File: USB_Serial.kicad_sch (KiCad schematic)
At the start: 1 part, among them U501 MCP2221A-I_SL

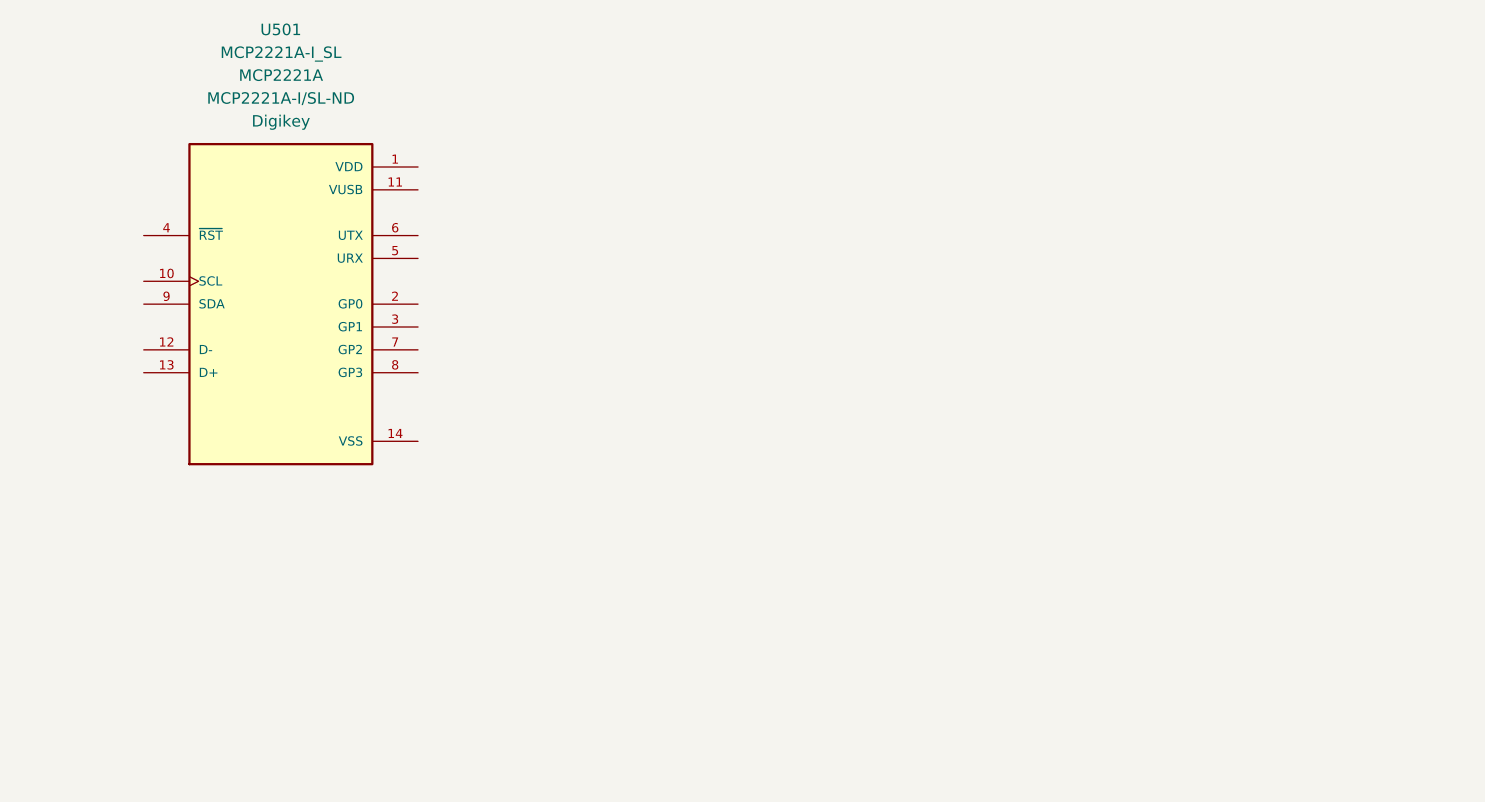
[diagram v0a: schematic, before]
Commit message: update schematic
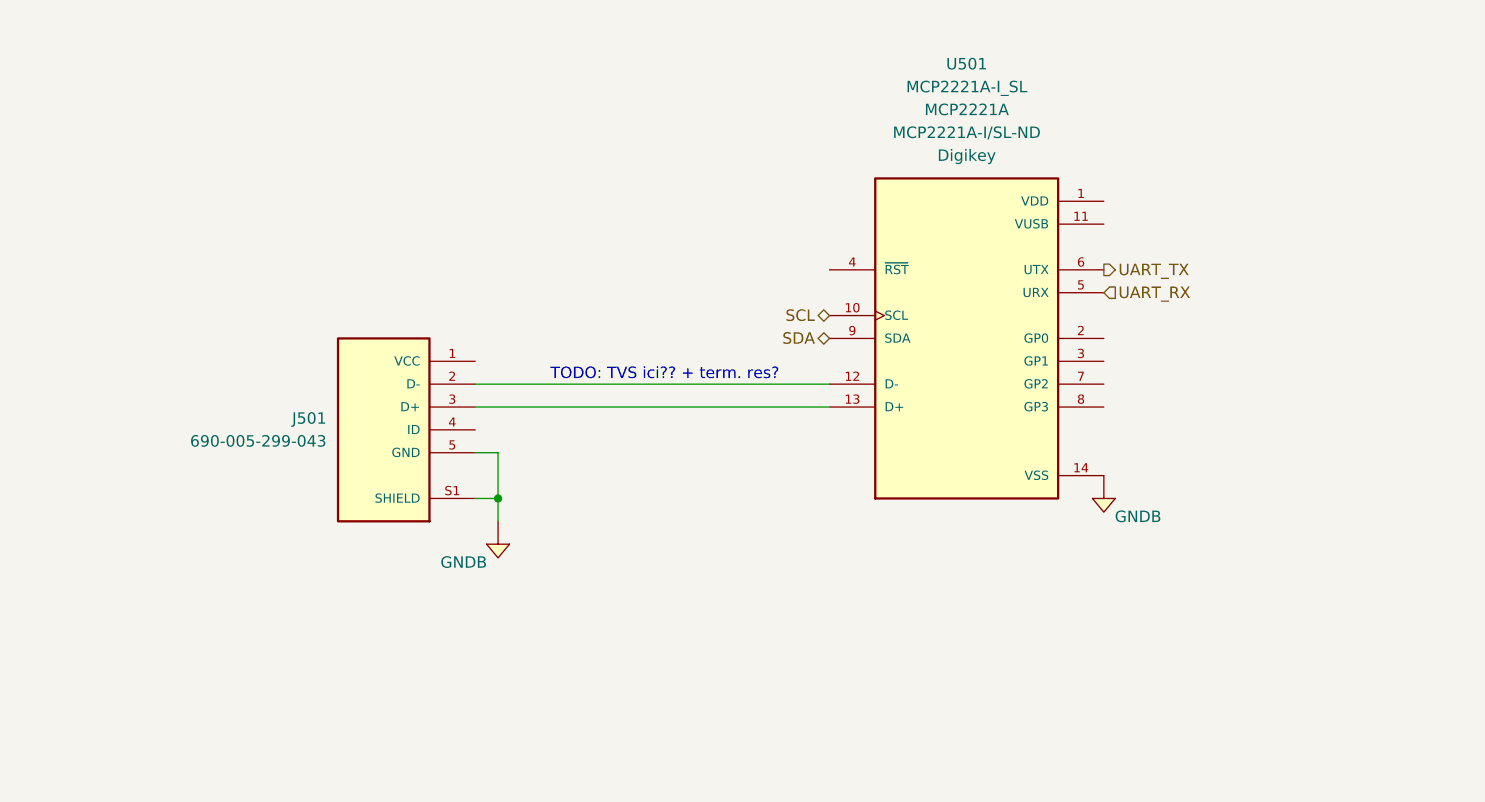
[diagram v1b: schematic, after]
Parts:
- added J501: 690-005-299-043, EDAC_690-005-299-043, symbol Connectors:690-005-299-043
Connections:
- net SCL: now reaches U501.10 (SCL)
- net at U501.12 (D-): now also J501.2 (D-)
- net at U501.13 (D+): now also J501.3 (D+)
- net GNDB: now reaches U501.14 (VSS)
- net GNDB: now also J501.5 (GND), J501.S1 (SHIELD)
- net UART_RX: now reaches U501.5 (URX)
- net UART_TX: now reaches U501.6 (UTX)
- net SDA: now reaches U501.9 (SDA)
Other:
- note added: "TODO: TVS ici?? + term. res?"
- moved on the sheet: U501

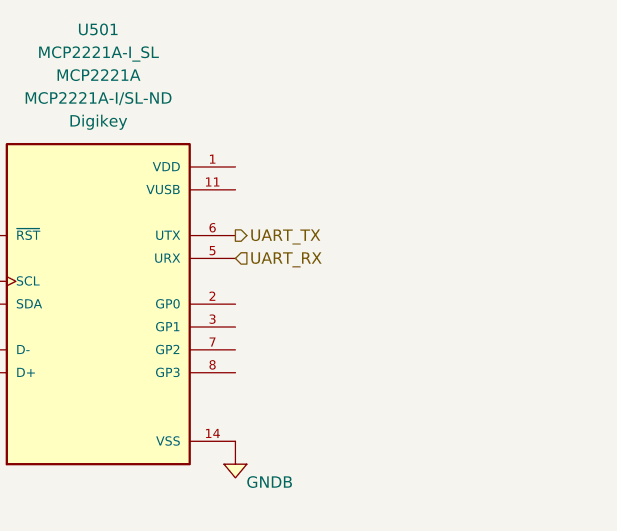
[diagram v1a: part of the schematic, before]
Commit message: update schematic
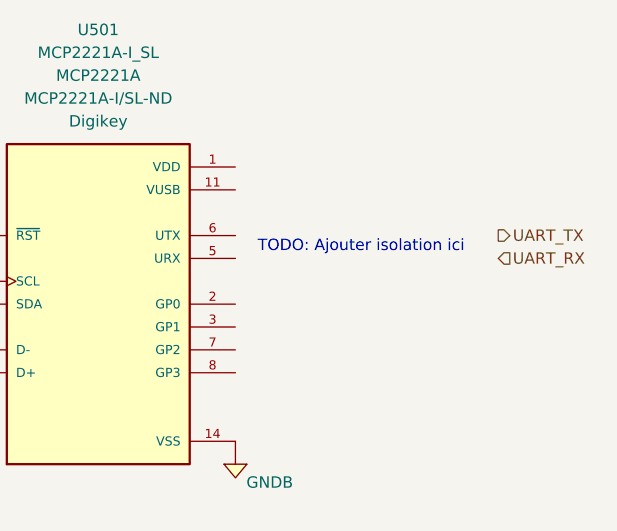
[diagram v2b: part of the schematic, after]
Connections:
- net UART_RX: no longer U501.5 (URX)
- net UART_TX: no longer U501.6 (UTX)
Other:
- note added: "TODO: Ajouter isolation ici"
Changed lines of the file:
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@@
+		)
+	)
+	(text "TODO: Ajouter isolation ici"
+		(exclude_from_sim no)
+		(at 199.39 71.12 0)
+		(effects
+			(font
+				(size 1.27 1.27)
+			)
 		)
 	)
@@
 	(hierarchical_label "UART_TX"
 		(shape output)
-		(at 185.42 69.85 0)
+		(at 214.63 69.85 0)
 		(fields_autoplaced yes)
 		(effects
@@
 	(hierarchical_label "UART_RX"
 		(shape input)
-		(at 185.42 72.39 0)
+		(at 214.63 72.39 0)
 		(fields_autoplaced yes)
 		(effects

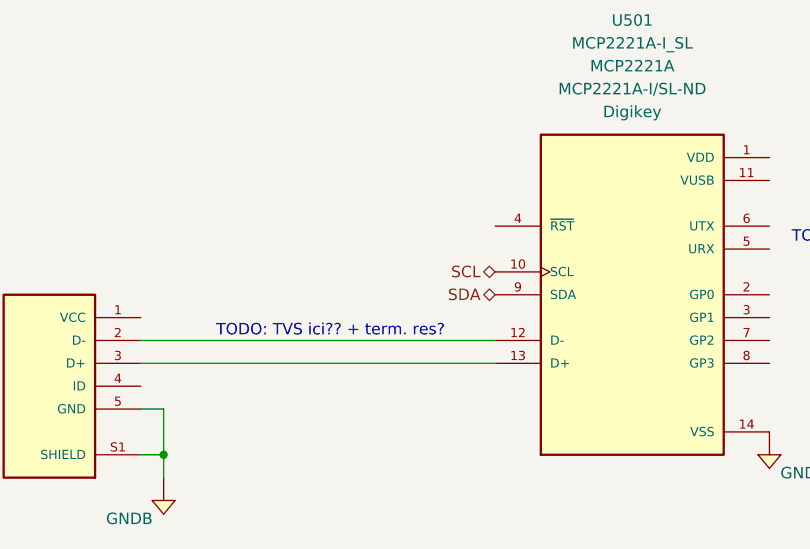
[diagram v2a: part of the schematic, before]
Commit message: update schematic
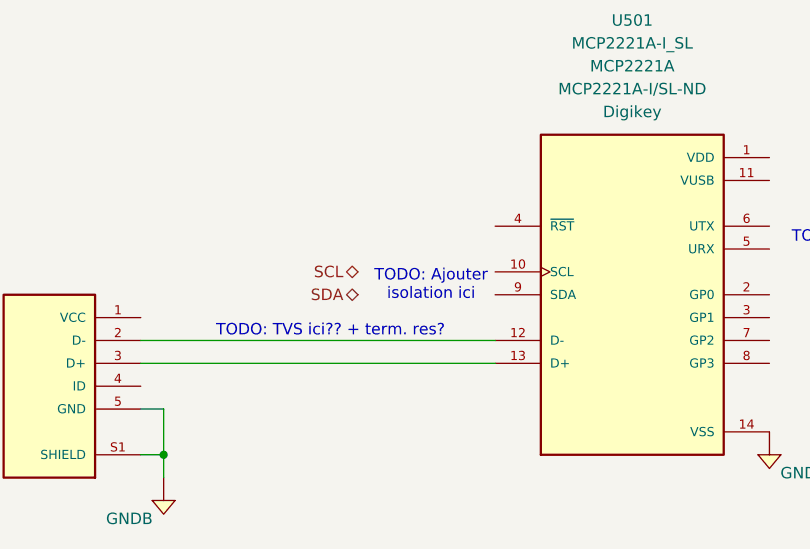
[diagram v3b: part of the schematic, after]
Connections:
- net SCL: no longer U501.10 (SCL)
- net SDA: no longer U501.9 (SDA)
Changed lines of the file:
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@@
+		)
+	)
+	(text "TODO: Ajouter \nisolation ici"
+		(exclude_from_sim no)
+		(at 147.828 76.454 0)
+		(effects
+			(font
+				(size 1.27 1.27)
+			)
 		)
 	)
@@
 	(hierarchical_label "SCL"
 		(shape bidirectional)
-		(at 154.94 74.93 180)
+		(at 139.7 74.93 180)
 		(fields_autoplaced yes)
 		(effects
@@
 	(hierarchical_label "SDA"
 		(shape bidirectional)
-		(at 154.94 77.47 180)
+		(at 139.7 77.47 180)
 		(fields_autoplaced yes)
 		(effects

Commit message: update schematique
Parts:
- added C24, C25: 885012207098, Capacitors:C0805, symbol Capacitors:885012207098
- added D12: 150080VS75000, Diodes:LED_0805_GREEN, symbol Diodes:150080VS75000
- added D13: 150080YS75000, Diodes:LED_0805_YELLOW, symbol Diodes:150080YS75000
- added J12: Header_Male_Pin_2.54mm_1X4_,_Unshrouded, Connectors:Headers_2.54mm_1X4, symbol Connectors:Header_Male_Pin_2.54mm_1X4_,_Unshrouded
- added R35, R36: RC0805JR-072K2L, Resistors:R0805, symbol Resistors:RC0805JR-072K2L
- added SB1, SB2: Solder_Bridge, Connectors:Solder_bridge_0805, symbol Connectors:Solder_Bridge
- renumbered J501 to J11, U501 to U10
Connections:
- net GNDB: now also C24.1, C25.1, D12.1 (Cathode), D13.1 (Cathode)
- net SCL: now also U10.10 (SCL)
- net SDA: now also U10.9 (SDA)
- net UART_RX: now also U10.5 (URX)
- net UART_TX: now also U10.6 (UTX)
- net USB_VBUS: now reaches J11.1 (VCC)
- net at J11.4 (ID): now also SB1.2, SB2.2
- net 3.3VB: now reaches U10.1 (VDD)
- net 3.3VB: now also C24.2
- net at U10.11 (VUSB): now also C25.2
- net GP0: now reaches U10.2 (GP0)
- net GP0: now also J12.1, R36.2
- net GP1: now reaches U10.3 (GP1)
- net GP1: now also J12.2, R35.2
- net RST_: now reaches U10.4 (~{RST})
- net GP2: now reaches U10.7 (GP2)
- net GP2: now also J12.3
- net GP3: now reaches U10.8 (GP3)
- net GP3: now also J12.4
- new net: D12.2 (Anode), R35.1
- new net: D13.2 (Anode), R36.1
- new net DGND: SB2.1
- new net USB_ID: SB1.1
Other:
- note added: "DO NOT CONNECT BOTH JUMPERS: DUAL MODE : SB12=0ohm, SB13=DNP NORMAL MODE: SB12=DNP, SB13=0ohm"
- note removed: "TODO: Ajouter isolation ici"
- note removed: "TODO: TVS ici?? + term. res?"
- moved on the sheet: J11, U10

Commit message: update schematique
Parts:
- renumbered C24 to C501, C25 to C502, D12 to D501, D13 to D502, J12 to J501, J11 to J502, R35 to R501, R36 to R502, SB1 to SB501, SB2 to SB502, U10 to U501
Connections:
- net 3.3VB renamed VDD
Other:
- note added: "RX"
- note added: "TX"
- title: (none) -> USB Serial
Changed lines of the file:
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@@
 	(generator_version "8.0")
 	(paper "USLetter")
+	(title_block
+		(title "USB Serial")
+		(comment 1 "Gérémy Sauvageau")
+	)
 	(junction
 		(at 148.59 54.61)
@@
 			)
 			(justify left bottom)
+		)
+	)
+	(text "TX"
+		(exclude_from_sim no)
+		(at 189.738 94.742 0)
+		(effects
+			(font
+				(size 1.27 1.27)
+			)
+		)
+	)
+	(text "RX"
+		(exclude_from_sim no)
+		(at 201.168 94.742 0)
+		(effects
+			(font
+				(size 1.27 1.27)
+			)
 		)
 	)
@@
 		(on_board yes)
 		(dnp no)
-		(property "Reference" "#PWR074"
+		(property "Reference" "#PWR0507"
 			(at 86.36 110.998 0)
 			(effects
@@
 			(project "SACE-HW"
 				(path "/4c1e5ca8-aa0f-4a8e-bffe-6765adb2e3e8/9ebd2496-8213-4575-b78a-e0103001acbf"
-					(reference "#PWR074")
+					(reference "#PWR0507")
 					(unit 1)
 				)
@@
 		(dnp no)
 		(fields_autoplaced yes)
-		(property "Reference" "C24"
+		(property "Reference" "C501"
 			(at 157.48 57.7849 90)
 			(effects
@@
 			(project "SACE-HW"
 				(path "/4c1e5ca8-aa0f-4a8e-bffe-6765adb2e3e8/9ebd2496-8213-4575-b78a-e0103001acbf"
-					(reference "C24")
+					(reference "C501")
 					(unit 1)
 				)
@@
 		(dnp no)
 		(fields_autoplaced yes)
-		(property "Reference" "D12"
+		(property "Reference" "D501"
 			(at 187.96 91.8209 90)
 			(effects
@@
 			(project "SACE-HW"
 				(path "/4c1e5ca8-aa0f-4a8e-bffe-6765adb2e3e8/9ebd2496-8213-4575-b78a-e0103001acbf"
-					(reference "D12")
+					(reference "D501")
 					(unit 1)
 				)
@@
 		(dnp no)
 		(fields_autoplaced yes)
-		(property "Reference" "J12"
+		(property "Reference" "J501"
 			(at 152.4 87.6299 0)
 			(effects
@@
 			(project "SACE-HW"
 				(path "/4c1e5ca8-aa0f-4a8e-bffe-6765adb2e3e8/9ebd2496-8213-4575-b78a-e0103001acbf"
-					(reference "J12")
+					(reference "J501")
 					(unit 1)
 				)
@@
 		(on_board yes)
 		(dnp no)
-		(property "Reference" "#PWR078"
+		(property "Reference" "#PWR0502"
 			(at 153.67 70.358 0)
 			(effects
@@
 			(project "SACE-HW"
 				(path "/4c1e5ca8-aa0f-4a8e-bffe-6765adb2e3e8/9ebd2496-8213-4575-b78a-e0103001acbf"
-					(reference "#PWR078")
+					(reference "#PWR0502")
 					(unit 1)
 				)
@@
 		(on_board yes)
 		(dnp no)
-		(property "Reference" "#PWR081"
+		(property "Reference" "#PWR0505"
 			(at 196.85 103.378 0)
 			(effects
@@
 			(project "SACE-HW"
 				(path "/4c1e5ca8-aa0f-4a8e-bffe-6765adb2e3e8/9ebd2496-8213-4575-b78a-e0103001acbf"
-					(reference "#PWR081")
+					(reference "#PWR0505")
 					(unit 1)
 				)
@@
 	)
 	(symbol
-		(lib_id "Power_Port:3.3VB")
+		(lib_id "Power_Port:VDD")
 		(at 148.59 54.61 0)
 		(unit 1)
@@
 		(dnp no)
 		(fields_autoplaced yes)
-		(property "Reference" "#PWR077"
+		(property "Reference" "#PWR0501"
 			(at 148.59 58.42 0)
 			(effects
@@
 			)
 		)
-		(property "Value" "3.3VB"
+		(property "Value" "VDD"
 			(at 148.59 49.53 0)
 			(effects
@@
 		)
 		(property "Datasheet" ""
-			(at 148.59 54.61 0)
+			(at 148.59 58.42 0)
 			(effects
 				(font
@@
 			(project "SACE-HW"
 				(path "/4c1e5ca8-aa0f-4a8e-bffe-6765adb2e3e8/9ebd2496-8213-4575-b78a-e0103001acbf"
-					(reference "#PWR077")
+					(reference "#PWR0501")
 					(unit 1)
 				)
@@
 		(on_board yes)
 		(dnp yes)
-		(property "Reference" "SB2"
+		(property "Reference" "SB502"
 			(at 107.95 116.84 0)
 			(effects
@@
 			(project "SACE-HW"
 				(path "/4c1e5ca8-aa0f-4a8e-bffe-6765adb2e3e8/9ebd2496-8213-4575-b78a-e0103001acbf"
-					(reference "SB2")
+					(reference "SB502")
 					(unit 1)
 				)
@@
 		(dnp no)
 		(fields_autoplaced yes)
-		(property "Reference" "R36"
+		(property "Reference" "R502"
 			(at 199.39 82.5499 90)
 			(effects
@@
 			(project "SACE-HW"
 				(path "/4c1e5ca8-aa0f-4a8e-bffe-6765adb2e3e8/9ebd2496-8213-4575-b78a-e0103001acbf"
-					(reference "R36")
+					(reference "R502")
 					(unit 1)
 				)
@@
 		(on_board yes)
 		(dnp no)
-		(property "Reference" "#PWR076"
+		(property "Reference" "#PWR0506"
 			(at 140.97 105.918 0)
 			(effects
@@
 			(project "SACE-HW"
 				(path "/4c1e5ca8-aa0f-4a8e-bffe-6765adb2e3e8/9ebd2496-8213-4575-b78a-e0103001acbf"
-					(reference "#PWR076")
+					(reference "#PWR0506")
 					(unit 1)
 				)
@@
 		(dnp no)
 		(fields_autoplaced yes)
-		(property "Reference" "C25"
+		(property "Reference" "C502"
 			(at 161.29 73.0249 90)
 			(effects
@@
 			(project "SACE-HW"
 				(path "/4c1e5ca8-aa0f-4a8e-bffe-6765adb2e3e8/9ebd2496-8213-4575-b78a-e0103001acbf"
-					(reference "C25")
+					(reference "C502")
 					(unit 1)
 				)
@@
 		(on_board yes)
 		(dnp no)
-		(property "Reference" "#PWR080"
+		(property "Reference" "#PWR0504"
 			(at 185.42 103.378 0)
 			(effects
@@
 			(project "SACE-HW"
 				(path "/4c1e5ca8-aa0f-4a8e-bffe-6765adb2e3e8/9ebd2496-8213-4575-b78a-e0103001acbf"
-					(reference "#PWR080")
+					(reference "#PWR0504")
 					(unit 1)
 				)
@@
 		(on_board yes)
 		(dnp no)
-		(property "Reference" "#PWR079"
+		(property "Reference" "#PWR0503"
 			(at 157.48 85.598 0)
 			(effects
@@
 			(project "SACE-HW"
 				(path "/4c1e5ca8-aa0f-4a8e-bffe-6765adb2e3e8/9ebd2496-8213-4575-b78a-e0103001acbf"
-					(reference "#PWR079")
+					(reference "#PWR0503")
 					(unit 1)
 				)
@@
 		(on_board yes)
 		(dnp no)
-		(property "Reference" "#PWR075"
+		(property "Reference" "#PWR0508"
 			(at 119.38 124.968 0)
 			(effects
@@
 			(project "SACE-HW"
 				(path "/4c1e5ca8-aa0f-4a8e-bffe-6765adb2e3e8/9ebd2496-8213-4575-b78a-e0103001acbf"
-					(reference "#PWR075")
+					(reference "#PWR0508")
 					(unit 1)
 				)
@@
 		(on_board yes)
 		(dnp no)
-		(property "Reference" "J11"
+		(property "Reference" "J502"
 			(at 76.2 82.296 0)
 			(effects
@@
 			(project "SACE-HW"
 				(path "/4c1e5ca8-aa0f-4a8e-bffe-6765adb2e3e8/9ebd2496-8213-4575-b78a-e0103001acbf"
-					(reference "J11")
+					(reference "J502")
 					(unit 1)
 				)
@@
 		(on_board yes)
 		(dnp no)
-		(property "Reference" "SB1"
+		(property "Reference" "SB501"
 			(at 107.95 109.22 0)
 			(effects
@@
 			(project "SACE-HW"
 				(path "/4c1e5ca8-aa0f-4a8e-bffe-6765adb2e3e8/9ebd2496-8213-4575-b78a-e0103001acbf"
-					(reference "SB1")
+					(reference "SB501")
 					(unit 1)
 				)
@@
 		(dnp no)
 		(fields_autoplaced yes)
-		(property "Reference" "D13"
+		(property "Reference" "D502"
 			(at 199.39 91.8209 90)
 			(effects
@@
 			(project "SACE-HW"
 				(path "/4c1e5ca8-aa0f-4a8e-bffe-6765adb2e3e8/9ebd2496-8213-4575-b78a-e0103001acbf"
-					(reference "D13")
+					(reference "D502")
 					(unit 1)
 				)
@@
 		(on_board yes)
 		(dnp no)
-		(property "Reference" "U10"
+		(property "Reference" "U501"
 			(at 125.984 61.976 0)
 			(effects
@@
 			(project "SACE-HW"
 				(path "/4c1e5ca8-aa0f-4a8e-bffe-6765adb2e3e8/9ebd2496-8213-4575-b78a-e0103001acbf"
-					(reference "U10")
+					(reference "U501")
 					(unit 1)
 				)
@@
 		(dnp no)
 		(fields_autoplaced yes)
-		(property "Reference" "R35"
+		(property "Reference" "R501"
 			(at 187.96 82.5499 90)
 			(effects
@@
 			(project "SACE-HW"
 				(path "/4c1e5ca8-aa0f-4a8e-bffe-6765adb2e3e8/9ebd2496-8213-4575-b78a-e0103001acbf"
-					(reference "R35")
+					(reference "R501")
 					(unit 1)
 				)
